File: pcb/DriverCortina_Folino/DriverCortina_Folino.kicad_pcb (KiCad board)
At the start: 2 copper layers, 90 x 50 mm, 34 parts, among them J1 AC 220v, J2 Llave Inversora, J3 Motor 1, J4 Motor 2, K1 G3MB-202PL-DC5, K2 G3MB-202PL-DC5, Q1 BC558, Q2 BC558, U1 ESP-01v090

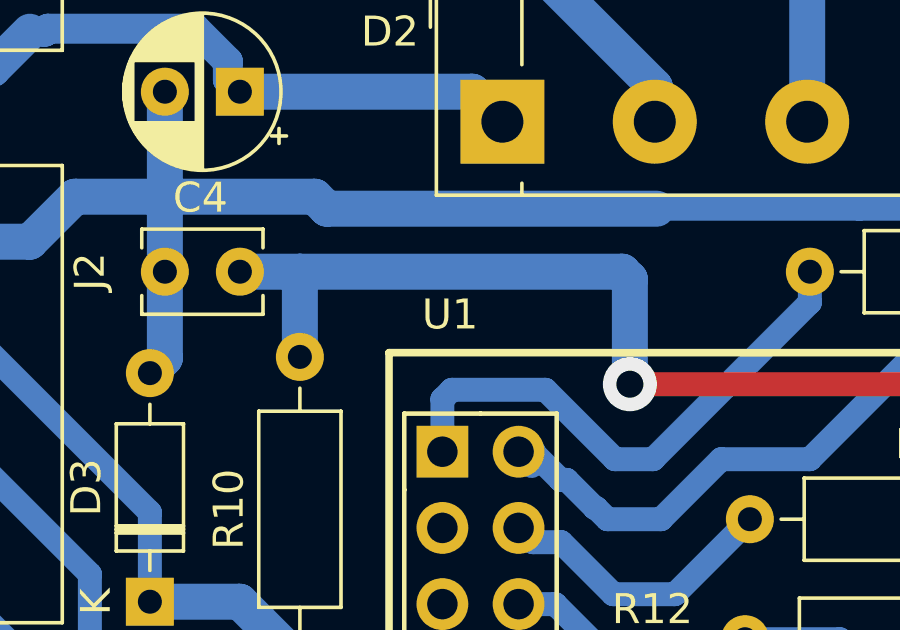
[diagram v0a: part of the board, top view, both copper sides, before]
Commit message: Se realizan las correciones del esquemático.
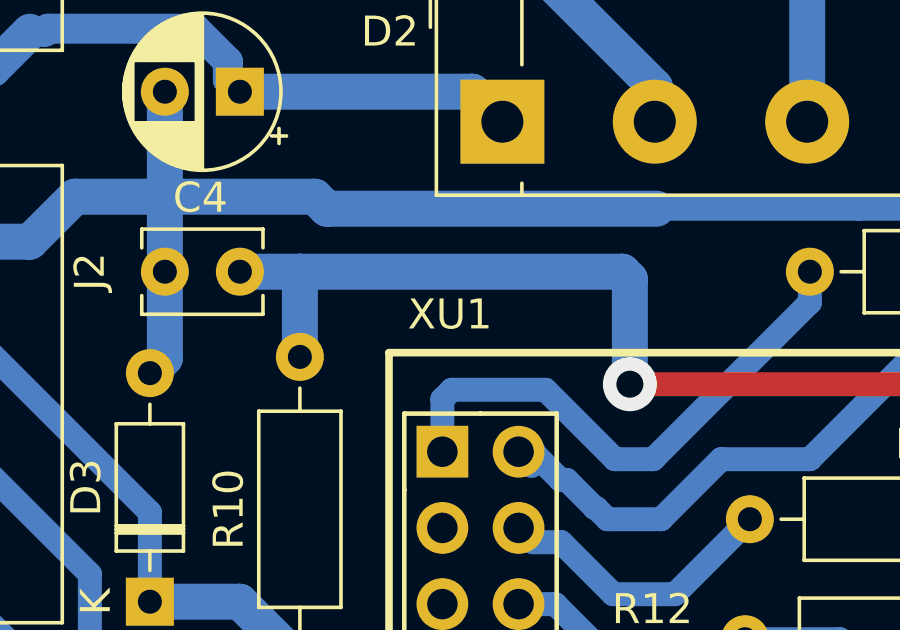
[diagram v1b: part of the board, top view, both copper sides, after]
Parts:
- C1: value C1uF -> 1uF
- C3: value C100uF -> 100uF
- C4: value C100nF -> 100nF
- F1, F2: value RXEF 065 -> RXEF065
- R1, R2, R5: value R100 -> 100
- R10, R11, R12, R6, R7, R8, R9: value R10K -> 10K
- R3, R4: value R1M -> 1M
- renumbered U1 to XU1

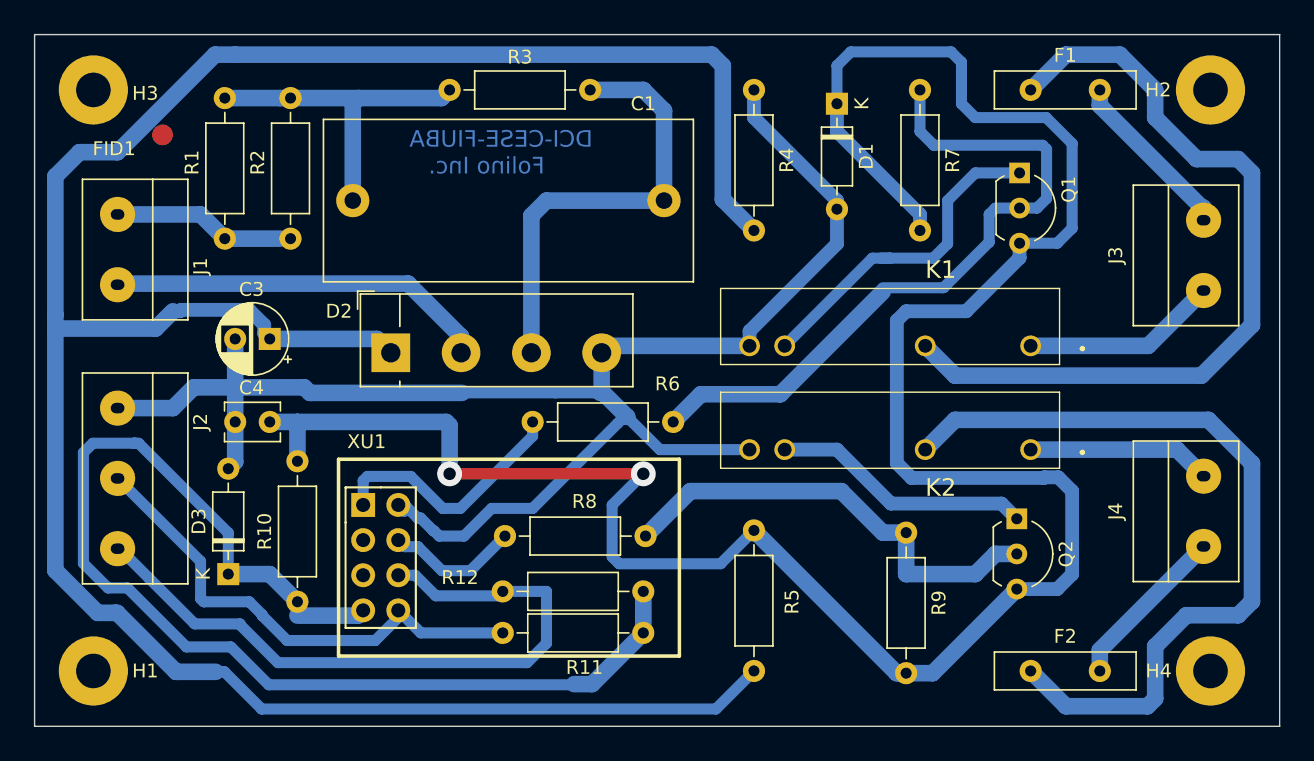
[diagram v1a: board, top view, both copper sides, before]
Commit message: Se actualiza PCB
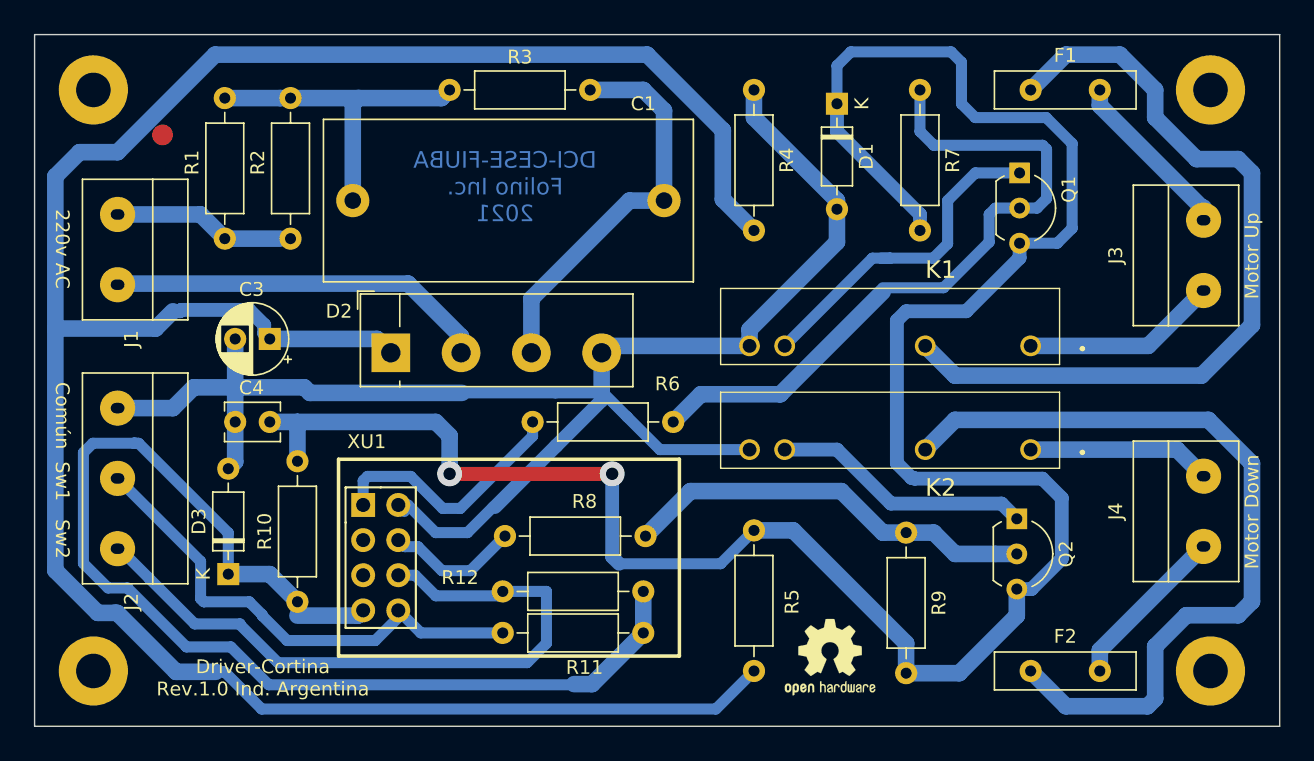
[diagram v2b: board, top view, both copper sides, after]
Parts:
- added REF**: OSHW-Logo2_7.3x6mm_SilkScreen, Symbol:OSHW-Logo2_7.3x6mm_SilkScreen, F.Cu at (164.5, 101.0)
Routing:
- net +5V: track 170.4 -> 166.7 mm
- net Net-(C1-Pad2): track 32.4 -> 28.9 mm
- net Net-(Q2-Pad2): track 33.5 -> 30.6 mm
- net Net-(C3-Pad1): track 175.8 -> 173.1 mm
- net GND: track 117.5 -> 116.6 mm
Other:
- net class Default: trace_width 0.25 -> 0.8
- rule trace_min: 0.2 -> 0.8
- rule via_min_size: 0.4 -> 0.8
- board text added: "220v AC"
- board text added: "============================= = Características = ============================= =Grillas 1 mm, 0,5mm, 0,25mm = =Vía: 1,8mm / 0,9mm = =Pistas: 1,2mm, 1mm, 0,8mm = =Margen: 0,25mm = =Dist. al borde: 0,8mm = =Documentación superficial: HASL = ============================="
- board text added: "Común Sw1 Sw2"
- board text added: "DCI-CESE-FIUBA Folino Inc. 2021"
- board text added: "Driver-Cortina Rev.1.0 Ind. Argentina"
- board text added: "Motor Down"
- board text added: "Motor Up"
- board text removed: "DCI-CESE-FIUBA Folino Inc."
- board text removed: "Grid; 1,00 mm Grid: 0,25 mm"

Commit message: Mejoras de PCB
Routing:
- net /Llave1: track 50.2 -> 49.7 mm

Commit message: Se corrigen detalles del PCB
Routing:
- added copper zone on B.Cu, net GND
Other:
- board text added: "============================= = Características = ============================= =Placa se simple faz = =En la capa F.Cu se intalan puentes = =Grillas 1 mm, 0,5mm, 0,25mm = =Vía: 1,8mm / 0,9mm = =Pistas: 1,2mm, 1mm, 0,8mm = =Margen: 0,50mm = =Dist. al borde: 0,8mm = =Documentación superficial: HASL = ============================="
- board text removed: "============================= = Características = ============================= =Grillas 1 mm, 0,5mm, 0,25mm = =Vía: 1,8mm / 0,9mm = =Pistas: 1,2mm, 1mm, 0,8mm = =Margen: 0,25mm = =Dist. al borde: 0,8mm = =Documentación superficial: HASL = ============================="
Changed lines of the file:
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@@
     (date 2021-04-19)
     (rev 1.2)
-    (company CESE_FIUBA)
-    (comment 1 "Profesor: Ing.  Diego Brengi")
-    (comment 2 "Revisor : Ing. Sergio Alberino")
-    (comment 3 "Autor: Ing. Pablo D. Folino")
+    (company "Licencia: http://creativecommons.org/licenses/by/4.0/")
+    (comment 1 CESE_FIUBA)
+    (comment 2 "Profesor: Ing.  Diego Brengi")
+    (comment 3 "Revisor : Ing. Sergio Alberino")
+    (comment 4 "Autor: Ing. Pablo D. Folino")
   )
   (layers
@@
     (user_trace_width 1.2)
     (trace_clearance 0.8)
-    (zone_clearance 0.508)
+    (zone_clearance 0.5)
     (zone_45_only no)
     (trace_min 0.8)
@@
     (add_net "Net-(XU1-Pad3)")
     (add_net "Net-(XU1-Pad5)")
+  )
+  (module ESP:ESP-01 (layer F.Cu)
+    (at 130.75 90)
+    (descr "Module, ESP-8266, ESP-01, 8 pin")
+    (tags "Module ESP-8266 ESP8266")
+    (fp_text reference XU1 (at 0.254 -4.572) (layer F.SilkS)
+      (effects (font (size 1 1) (thickness 0.15)))
+    )
+    (fp_text value ESP-01v090 (at 12.192 3.556) (layer F.Fab)
+      (effects (font (size 1 1) (thickness 0.15)))
+    )
+    (fp_line (start -1.778 -3.302) (end 22.86 -3.302) (layer F.SilkS) (width 0.254))
+    (fp_line (start 22.86 -3.302) (end 22.86 10.922) (layer F.SilkS) (width 0.254))
+    (fp_line (start 22.86 10.922) (end -1.778 10.922) (layer F.SilkS) (width 0.254))
+    (fp_line (start -1.778 10.922) (end -1.778 -3.302) (layer F.SilkS) (width 0.254))
+    (fp_line (start -1.778 -3.302) (end 22.86 -3.302) (layer F.Fab) (width 0.05))
+    (fp_line (start 22.86 -3.302) (end 22.86 10.922) (layer F.Fab) (width 0.05))
+    (fp_line (start 22.86 10.922) (end -1.778 10.922) (layer F.Fab) (width 0.05))
+    (fp_line (start -1.778 10.922) (end -1.778 -3.302) (layer F.Fab) (width 0.05))
+    (fp_line (start 1.27 -1.27) (end -1.27 -1.27) (layer F.SilkS) (width 0.1524))
+    (fp_line (start -1.27 -1.27) (end -1.27 1.27) (layer F.SilkS) (width 0.1524))
+    (fp_line (start -1.75 -1.75) (end -1.75 9.4) (layer F.CrtYd) (width 0.05))
+    (fp_line (start 4.3 -1.75) (end 4.3 9.4) (layer F.CrtYd) (width 0.05))
+    (fp_line (start -1.75 -1.75) (end 4.3 -1.75) (layer F.CrtYd) (width 0.05))
+    (fp_line (start -1.75 9.4) (end 4.3 9.4) (layer F.CrtYd) (width 0.05))
+    (fp_line (start -1.27 1.27) (end -1.27 8.89) (layer F.SilkS) (width 0.1524))
+    (fp_line (start -1.27 8.89) (end 3.81 8.89) (layer F.SilkS) (width 0.1524))
+    (fp_line (start 3.81 8.89) (end 3.81 -1.27) (layer F.SilkS) (width 0.1524))
+    (fp_line (start 3.81 -1.27) (end 1.27 -1.27) (layer F.SilkS) (width 0.1524))
+    (pad 8 thru_hole oval (at 2.54 7.62) (size 1.7272 1.7272) (drill 1.016) (layers *.Cu *.Mask F.SilkS)
+      (net 11 /Llave2))
+    (pad 7 thru_hole oval (at 0 7.62) (size 1.7272 1.7272) (drill 1.016) (layers *.Cu *.Mask F.SilkS)
+      (net 21 +3V3))
+    (pad 6 thru_hole oval (at 2.54 5.08) (size 1.7272 1.7272) (drill 1.016) (layers *.Cu *.Mask F.SilkS)
+      (net 12 /Llave1))
+    (pad 5 thru_hole oval (at 0 5.08) (size 1.7272 1.7272) (drill 1.016) (layers *.Cu *.Mask F.SilkS)
+      (net 23 "Net-(XU1-Pad5)"))
+    (pad 4 thru_hole oval (at 2.54 2.54) (size 1.7272 1.7272) (drill 1.016) (layers *.Cu *.Mask F.SilkS)
+      (net 19 /Out2))
+    (pad 3 thru_hole oval (at 0 2.54) (size 1.7272 1.7272) (drill 1.016) (layers *.Cu *.Mask F.SilkS)
+      (net 24 "Net-(XU1-Pad3)"))
+    (pad 2 thru_hole oval (at 2.54 0) (size 1.7272 1.7272) (drill 1.016) (layers *.Cu *.Mask F.SilkS)
+      (net 3 GND))
+    (pad 1 thru_hole rect (at 0 0) (size 1.7272 1.7272) (drill 1.016) (layers *.Cu *.Mask F.SilkS)
+      (net 18 /Out1))
+    (model ${KISYS3DMOD}/Connector_PinSocket_2.54mm.3dshapes/PinSocket_2x04_P2.54mm_Vertical.wrl
+      (offset (xyz 2.54 0 0))
+      (scale (xyz 1 1 1))
+      (rotate (xyz 0 0 0))
+    )
+    (model /home/pablo/Documentos/Especialización/12_DCI/Proyectos/ESP_01.wrl
+      (offset (xyz -0.75 -11 9))
+      (scale (xyz 0.3937 0.3937 0.3937))
+      (rotate (xyz 0 0 0))
+    )
   )
   (module Symbol:OSHW-Logo2_7.3x6mm_SilkScreen (layer F.Cu)
@@
       (xy -0.113933 -2.757629) (xy -0.013056 -2.757714) (xy 0 -2.757714) (xy 0.10391 -2.757652)) (layer F.SilkS) (width 0.01))
   )
-  (module ESP:ESP-01 (layer F.Cu)
-    (at 130.75 90)
-    (descr "Module, ESP-8266, ESP-01, 8 pin")
-    (tags "Module ESP-8266 ESP8266")
-    (fp_text reference XU1 (at 0.254 -4.572) (layer F.SilkS)
-      (effects (font (size 1 1) (thickness 0.15)))
-    )
-    (fp_text value ESP-01v090 (at 12.192 3.556) (layer F.Fab)
-      (effects (font (size 1 1) (thickness 0.15)))
-    )
-    (fp_line (start -1.778 -3.302) (end 22.86 -3.302) (layer F.SilkS) (width 0.254))
-    (fp_line (start 22.86 -3.302) (end 22.86 10.922) (layer F.SilkS) (width 0.254))
-    (fp_line (start 22.86 10.922) (end -1.778 10.922) (layer F.SilkS) (width 0.254))
-    (fp_line (start -1.778 10.922) (end -1.778 -3.302) (layer F.SilkS) (width 0.254))
-    (fp_line (start -1.778 -3.302) (end 22.86 -3.302) (layer F.Fab) (width 0.05))
-    (fp_line (start 22.86 -3.302) (end 22.86 10.922) (layer F.Fab) (width 0.05))
-    (fp_line (start 22.86 10.922) (end -1.778 10.922) (layer F.Fab) (width 0.05))
-    (fp_line (start -1.778 10.922) (end -1.778 -3.302) (layer F.Fab) (width 0.05))
-    (fp_line (start 1.27 -1.27) (end -1.27 -1.27) (layer F.SilkS) (width 0.1524))
-    (fp_line (start -1.27 -1.27) (end -1.27 1.27) (layer F.SilkS) (width 0.1524))
-    (fp_line (start -1.75 -1.75) (end -1.75 9.4) (layer F.CrtYd) (width 0.05))
-    (fp_line (start 4.3 -1.75) (end 4.3 9.4) (layer F.CrtYd) (width 0.05))
-    (fp_line (start -1.75 -1.75) (end 4.3 -1.75) (layer F.CrtYd) (width 0.05))
-    (fp_line (start -1.75 9.4) (end 4.3 9.4) (layer F.CrtYd) (width 0.05))
-    (fp_line (start -1.27 1.27) (end -1.27 8.89) (layer F.SilkS) (width 0.1524))
-    (fp_line (start -1.27 8.89) (end 3.81 8.89) (layer F.SilkS) (width 0.1524))
-    (fp_line (start 3.81 8.89) (end 3.81 -1.27) (layer F.SilkS) (width 0.1524))
-    (fp_line (start 3.81 -1.27) (end 1.27 -1.27) (layer F.SilkS) (width 0.1524))
-    (pad 8 thru_hole oval (at 2.54 7.62) (size 1.7272 1.7272) (drill 1.016) (layers *.Cu *.Mask F.SilkS)
-      (net 11 /Llave2))
-    (pad 7 thru_hole oval (at 0 7.62) (size 1.7272 1.7272) (drill 1.016) (layers *.Cu *.Mask F.SilkS)
-      (net 21 +3V3))
-    (pad 6 thru_hole oval (at 2.54 5.08) (size 1.7272 1.7272) (drill 1.016) (layers *.Cu *.Mask F.SilkS)
-      (net 12 /Llave1))
-    (pad 5 thru_hole oval (at 0 5.08) (size 1.7272 1.7272) (drill 1.016) (layers *.Cu *.Mask F.SilkS)
-      (net 23 "Net-(XU1-Pad5)"))
-    (pad 4 thru_hole oval (at 2.54 2.54) (size 1.7272 1.7272) (drill 1.016) (layers *.Cu *.Mask F.SilkS)
-      (net 19 /Out2))
-    (pad 3 thru_hole oval (at 0 2.54) (size 1.7272 1.7272) (drill 1.016) (layers *.Cu *.Mask F.SilkS)
-      (net 24 "Net-(XU1-Pad3)"))
-    (pad 2 thru_hole oval (at 2.54 0) (size 1.7272 1.7272) (drill 1.016) (layers *.Cu *.Mask F.SilkS)
-      (net 3 GND))
-    (pad 1 thru_hole rect (at 0 0) (size 1.7272 1.7272) (drill 1.016) (layers *.Cu *.Mask F.SilkS)
-      (net 18 /Out1))
-    (model ${KISYS3DMOD}/Connector_PinSocket_2.54mm.3dshapes/PinSocket_2x04_P2.54mm_Vertical.wrl
-      (offset (xyz 2.54 0 0))
-      (scale (xyz 1 1 1))
-      (rotate (xyz 0 0 0))
-    )
-  )
   (module SSR:G3MB202PLDC5 (layer F.Cu)
     (at 179 86)
@@
   (gr_line (start 107 106) (end 107 56) (layer Edge.Cuts) (width 0.1))
   (gr_line (start 107 56) (end 197 56) (layer Edge.Cuts) (width 0.1))
-  (gr_text "=============================\n=          Características                   =\n=============================\n=Grillas 1 mm, 0,5mm, 0,25mm             = \n=Vía: 1,8mm /  0,9mm                      =\n=Pistas: 1,2mm, 1mm, 0,8mm               =\n=Margen: 0,25mm                           =\n=Dist. al borde: 0,8mm                      =\n=Documentación superficial: HASL           =\n=============================" (at 61 78) (layer Dwgs.User)
+  (gr_text "=============================\n=          Características                   =\n=============================\n=Placa se simple faz                        =\n=En la capa F.Cu se intalan puentes        =\n=Grillas 1 mm, 0,5mm, 0,25mm             = \n=Vía: 1,8mm /  0,9mm                      =\n=Pistas: 1,2mm, 1mm, 0,8mm               =\n=Margen: 0,50mm                           =\n=Dist. al borde: 0,8mm                      =\n=Documentación superficial: HASL           =\n=============================\n" (at 61 78) (layer Dwgs.User)
     (effects (font (size 1 1) (thickness 0.15)) (justify left))
   )
@@
   (segment (start 113 69) (end 119 69) (width 1.2) (layer B.Cu) (net 22))
   (segment (start 120.75 70.75) (end 124.75 70.75) (width 1.2) (layer B.Cu) (net 22))
+  (zone (net 3) (net_name GND) (layer B.Cu) (hatch edge 0.508)
+    (connect_pads (clearance 0.5))
+    (min_thickness 0.3)
+    (fill yes (arc_segments 32) (thermal_gap 0.5) (thermal_bridge_width 0.5))
+    (polygon
+      (pts
+        (xy 197.5 106.5) (xy 106.5 106.5) (xy 106.5 55.5) (xy 197.5 55.5)
+      )
+    )
+  )
 )
